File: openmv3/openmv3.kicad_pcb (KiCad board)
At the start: 4 copper layers, 35.6 x 44.5 mm, 58 parts, among them M1 9774030243R, M2 9774030243R, Q1 BSS138, Q2 Si2301BDS, U1 STM32H743VIT6, U5 TPS731XX, U8 PAM2305AABADJ, X1 MF-CON-MICROUSB-RIGHT, X2 USD-1040310811, X3 DF12-36-DS, X4 S2B-PH-K-S(LF)(SN), Y1 7S-12.000MAHE-T

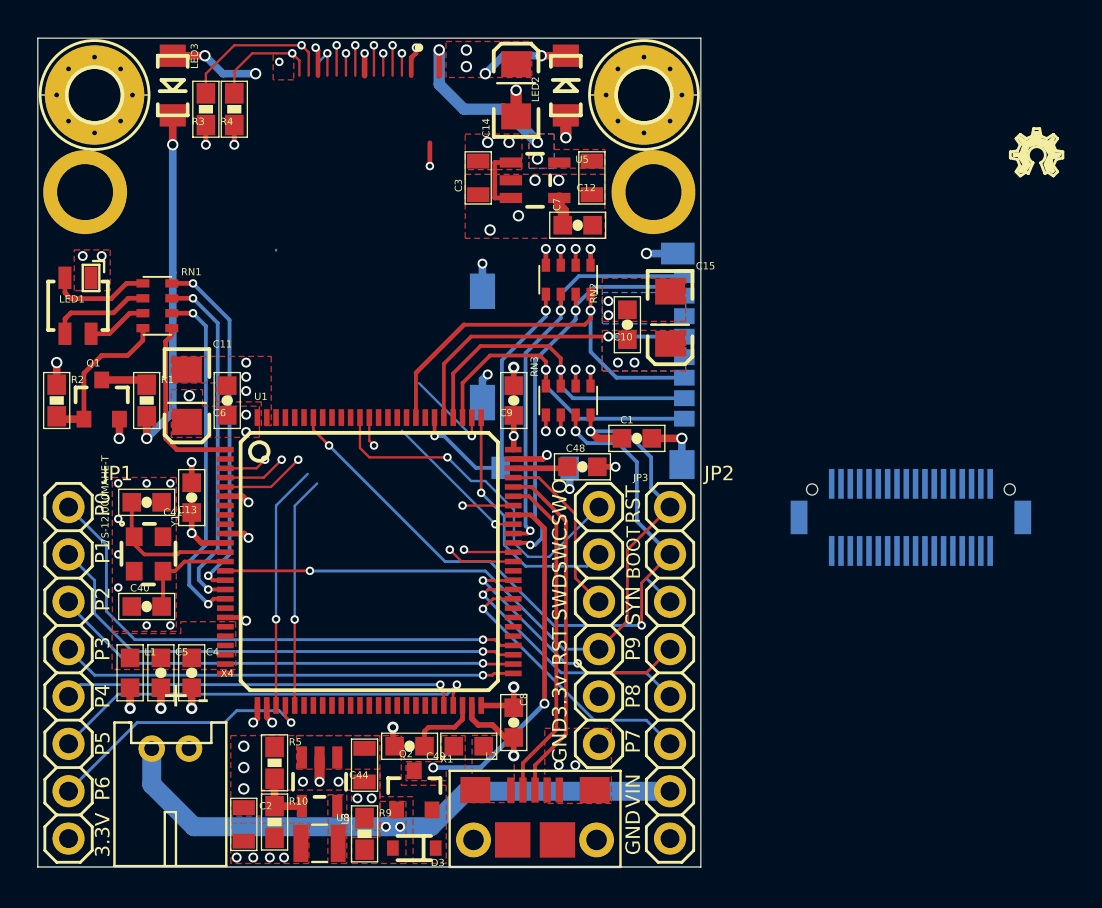
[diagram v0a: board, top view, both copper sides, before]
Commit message: Found diffs MV3 to MV4 for direct mount
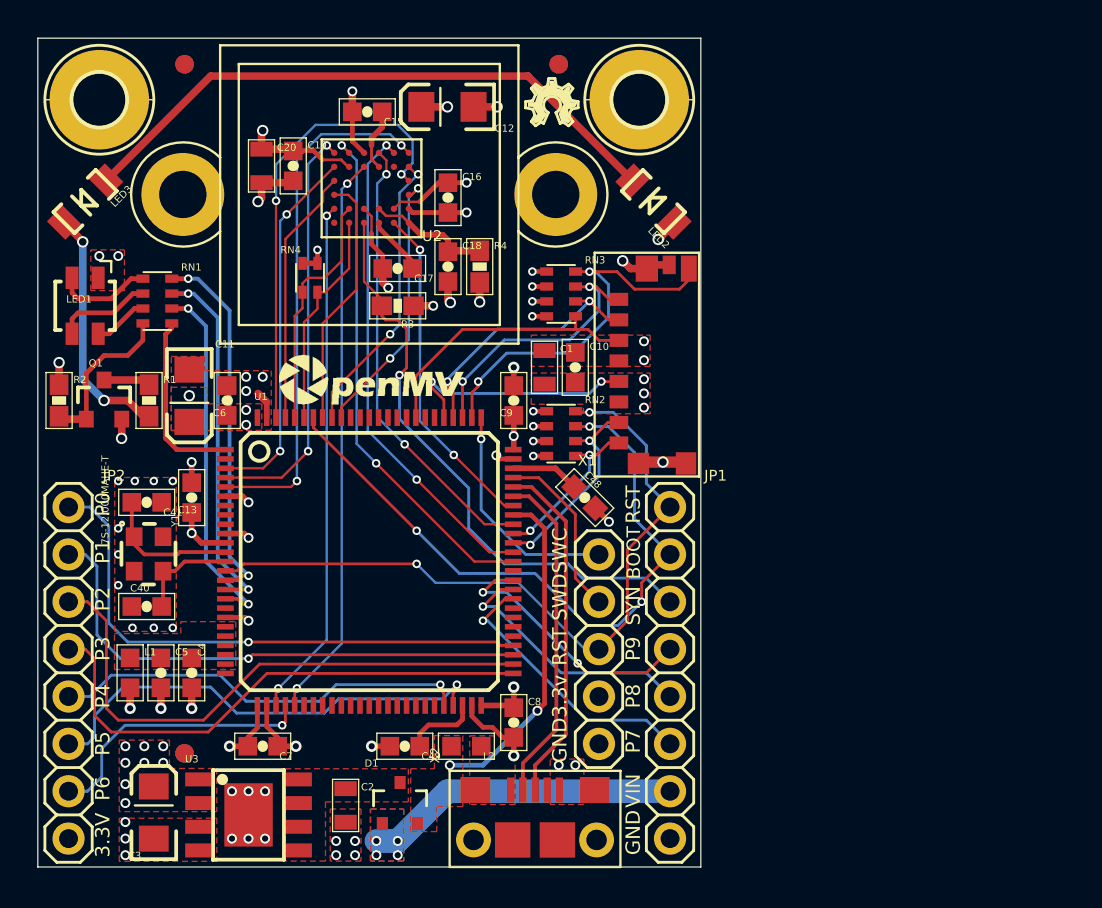
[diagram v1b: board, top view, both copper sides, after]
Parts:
- removed C14: 47uF, base:EIA3216
- removed C44: 22uF, base:0805
- removed D3: SDM2U20SD3-7, base:SOD-323
- removed L3: 4.7uH/1.4A, base:1007
- removed M1, M2: 9774030243R, base:9774030151R
- removed Q2: Si2301BDS, base:SOT23-3
- removed R10: 453K, base:0603-RES
- removed R5: 100K, base:0603-RES
- removed R9: 10K, base:0603-RES
- removed U5: TPS731XX, base:SOT23-5
- removed U8: PAM2305AABADJ, base:TSOT25
- removed X3: DF12-36-DS, base:DF12-36-DS
- removed X4: S2B-PH-K-S(LF)(SN), base:JST-PH-2-THM-RA
- added C16: 0.1uF, openmv3:0603-CAP, F.Cu at (152.7, 91.3)
- added C17: 0.1uF, openmv3:0603-CAP, F.Cu at (150.0, 95.1)
- added C18: 4.7uF, openmv3:0603-CAP, F.Cu at (152.7, 95.0)
- added C19: 0.1uF, openmv3:0603-CAP, F.Cu at (144.4, 89.6)
- added C20: 22uF, openmv3:0805, F.Cu at (142.7, 89.6)
- added D1: PMEG2005CT, openmv3:SOT23, F.Cu at (150.2, 123.8)
- added F1: FIDUCIAL1X2, openmv3:FIDUCIAL-1X2, F.Cu at (138.6, 121.1)
- added F2: FIDUCIAL1X2, openmv3:FIDUCIAL-1X2, F.Cu at (138.6, 84.2)
- added F3: FIDUCIAL1X2, openmv3:FIDUCIAL-1X2, F.Cu at (158.7, 84.2)
- added F4: FIDUCIAL1X2, openmv3:FIDUCIAL-1X2, B.Cu at (138.6, 121.1)
- added F5: FIDUCIAL1X2, openmv3:FIDUCIAL-1X2, B.Cu at (138.6, 84.2)
- added F6: FIDUCIAL1X2, openmv3:FIDUCIAL-1X2, B.Cu at (158.7, 84.2)
- added LM1: LENSMOUNT20MM, openmv3:LENSMOUNT-20MM, F.Cu at (148.5, 91.2)
- added RN4: 4.7K, openmv3:EXBV4V, F.Cu at (145.3, 95.6)
- added U$4: , openmv3:OMV-LOGO-SMALL, F.Cu at (143.5, 102.6)
- added U2: OV7725, openmv3:CSP2-28, F.Cu at (148.6, 90.8)
- added U3: BD33IA, openmv3:HTSOP-J8, F.Cu at (142.0, 124.4)
- C1: value 1uF -> 22uF; footprint base:0603-CAP -> openmv3:0805
- C10, C13, C4, C40, C41, C48, C49, C5, C6, C7, C8, C9: footprint base:0603-CAP -> openmv3:0603-CAP
- C11: footprint base:EIA3216 -> openmv3:EIA3216
- C12, C3: value 10uF -> 47uF; footprint base:0805 -> openmv3:EIA3216
- C15: value 47uF -> 0.1uF; footprint base:EIA3216 -> openmv3:0603-CAP
- C2: footprint base:0805 -> openmv3:0805
- H1, H2: footprint base:2,8-PAD -> openmv3:2,8-PAD
- JP1, JP2: footprint base:1X08 -> openmv3:1X08
- JP3: value PINHD-1X6 -> PINHD-1X5; footprint base:1X06 -> openmv3:1X05
- L1, L2: footprint base:0603 -> openmv3:0603
- LED1: footprint base:LED-TRICOLOR-SMD-MF -> openmv3:LED-TRICOLOR-SMD-MF
- LED2, LED3: footprint base:LED-1206 -> openmv3:LED-1206
- LOGO1: footprint base:OSHW_FILLX100_NOTEXT -> openmv3:OSHW_FILLX100_NOTEXT
- Q1: value BSS138 -> MOSFET; footprint base:SOT23-3 -> openmv3:SOT23-3
- R1: footprint base:0603-RES -> openmv3:0603-RES
- R2: value 10K -> 10k; footprint base:0603-RES -> openmv3:0603-RES
- R3: value 4.7K -> 10k; footprint base:0603-RES -> openmv3:0603-RES
- R4: value 4.7K -> 4.7R; footprint base:0603-RES -> openmv3:0603-RES
- RN1, RN2, RN3: footprint base:EXBV8V -> openmv3:EXBV8V
- U$1: footprint base:WEEE -> openmv3:WEEE
- U$2: footprint base:ROHS -> openmv3:ROHS
- U$3: footprint base:OMV-LOGO -> openmv3:OMV-LOGO
- U1: value STM32H743VIT6 -> STM32F765VGT6; footprint base:LQFP100 -> openmv3:LQFP100
- X1: value MF-CON-MICROUSB-RIGHT -> 47571-0001; footprint base:MICROUSB-RIGHT -> openmv3:USD-47571
- X2: value USD-1040310811 -> MF-CON-MICROUSB-RIGHT; footprint base:1040310811 -> openmv3:MICROUSB-RIGHT; moved to F.Cu
- Y1: footprint base:CRYSTAL-2.5X2.0 -> openmv3:CRYSTAL-2.5X2.0
- moved C3 38.2 mm to (136.9, 124.3)
- moved C7 32.6 mm to (142.8, 120.8), turned to 180 degrees
- moved JP1 32.3 mm to (164.6, 116.8)
- moved JP2 32.3 mm to (132.4, 116.8)
- moved X2 31.4 mm to (157.4, 124.4), turned to 0 degrees
- moved LOGO1 26.1 mm to (156.9, 87.5)
- moved X1 24.5 mm to (163.5, 100.7), turned to 90 degrees
- moved C15 19.6 mm to (148.4, 86.7), turned to 180 degrees
- moved R4 15.6 mm to (154.4, 95.0), turned to 270 degrees
- moved R3 14.7 mm to (150.0, 97.1), turned to 180 degrees
- moved C12 8.63 mm to (152.7, 86.5), turned to 180 degrees
- moved RN2 8.26 mm to (158.8, 104.0), turned to 270 degrees
- moved LED3 7.80 mm to (133.3, 91.5), turned to 225 degrees
- moved LED2 7.80 mm to (163.7, 91.5), turned to 135 degrees
- moved C1 6.25 mm to (157.9, 100.4), turned to 270 degrees
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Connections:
- net /GPIO1 renamed Net-(U1-Pad84)
- net /GPIO2 renamed Net-(U1-Pad85)
- net /GPIO3 renamed Net-(U1-Pad82)
- net /UART2_RX renamed Net-(U1-Pad87)
- net /UART2_TX renamed Net-(U1-Pad86)
- C1 pad 1: /NRST -> VCC
- C2 pad 1: GND -> VIN
- C2 pad 2: VCC -> GND
- C7 pad 1: Net-(C7-Pad1) -> VCC
- JP1 pad 1: /SPI2_MOSI -> /NRST
- JP1 pad 2: /SPI2_MISO -> /BOOT0
- JP1 pad 3: /SPI2_SCLK -> /FSIN
- JP1 pad 4: /SPI2_NSS -> /TIM4_CH3
- JP1 pad 5: /I2C2_SCL -> /TIM4_CH2
- JP1 pad 6: /I2C2_SDA -> /TIM4_CH1
- JP1 pad 7: /DAC -> RAW
- JP1 pad 8: VCC -> GND
- JP2 pad 1: /NRST -> /SPI2_MOSI
- JP2 pad 2: /BOOT0 -> /SPI2_MISO
- JP2 pad 3: /DCMI_FSIN -> /SPI2_SCLK
- JP2 pad 4: /TIM4_CH3 -> /SPI2_NSS
- JP2 pad 5: /TIM4_CH2 -> /I2C2_SCL
- JP2 pad 6: /TIM4_CH1 -> /I2C2_SDA
- JP2 pad 7: VIN -> /DAC
- JP2 pad 8: GND -> VCC
- JP3 pad 1: /SPI3_SCLK/TRACESWO -> /SWCLK
- JP3 pad 2: /SWCLK -> /SWDIO
- JP3 pad 3: /SWDIO -> /NRST
- JP3 pad 4: /NRST -> VCC
- JP3 pad 5: VCC -> GND
- R3 pad 1: VCC -> GND
- R3 pad 2: /I2C1_SCL -> /FSIN
- R4 pad 1: VCC -> Net-(C18-Pad1)
- R4 pad 2: /I2C1_SDA -> VCC
- RN2 pad 2: VCC -> GND
- RN2 pad 5: /SD_CD -> /SDIO_D1
- RN2 pad 6: /SDIO_D1 -> /SDIO_D0
- RN2 pad 7: /SDIO_D0 -> /BOOT0
- RN2 pad 8: /SDIO_CMD -> /NRST
- RN3 pad 3: /BOOT0 -> VCC
- RN3 pad 4: /NRST -> VCC
- RN3 pad 5: VCC -> /SDIO_CMD
- RN3 pad 6: GND -> /SDIO_D3
- RN3 pad 7: /SDIO_D3 -> /SDIO_D2
- RN3 pad 8: /SDIO_D2 -> /SD_CD
- U1 pad 77: /SPI3_SSEL -> /SD_CD
- U1 pad 81: /SD_CD -> Net-(U1-Pad81)
- U1 pad 88: /DCMI_PWDN -> Net-(U1-Pad88)
- U1 pad 89: /SPI3_SCLK/TRACESWO -> Net-(U1-Pad89)
- U1 pad 90: /SPI3_MISO -> Net-(U1-Pad90)
- U1 pad 91: /SPI3_MOSI -> /DCMI_PWDN
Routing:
- net /FSIN: track 0.00 -> 31.8 mm, vias 0 -> 1
- net VIN: track 31.4 -> 0.00 mm, vias 2 -> 0
- net /DCMI_D3: track 0.03 -> 24.8 mm, vias 0 -> 2
- net /DCMI_D0: track 3.67 -> 27.9 mm, vias 1 -> 2
- net /DCMI_D7: track 6.14 -> 28.3 mm
- net /DCMI_D1: track 4.66 -> 26.8 mm
- net /SPI3_SCLK/TRACESWO: track 19.0 -> 0.00 mm, vias 1 -> 0
- net /DCMI_D6: track 4.62 -> 22.4 mm
- net RAW: track 0.00 -> 16.9 mm, vias 0 -> 4
- net /DCMI_PCLK: track 14.0 -> 30.4 mm
- net /DCMI_D4: track 3.95 -> 19.8 mm
- net /DCMI_D5: track 0.00 -> 15.6 mm, vias 0 -> 2
- net /DCMI_RST: track 2.72 -> 18.1 mm, vias 1 -> 2
- net /DCMI_CLK: track 9.24 -> 24.2 mm
- net GND: track 32.1 -> 46.6 mm, vias 48 -> 54
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- added copper zone on B.Cu, net RAW
- removed copper zone on B.Cu, net GND
- removed copper zone on F.Cu, net Net-(L3-Pad1)
- removed copper zone on B.Cu, net VCC
- removed copper zone on B.Cu, net VDDA
- removed copper zone on F.Cu, net VDDA
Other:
- board text added: "10/15/2016"
- board text added: "OV7725-M7"
- board text added: "OpenMV3 R1"
- board text removed: "10/27/18"
- board text removed: "OpenMV-H7 R1"
- board text removed: "SWO"
